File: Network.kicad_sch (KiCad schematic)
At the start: 32 parts, among them J6 RJ45_HR913550A, U1 IMX6UL, U11 RTL8201F

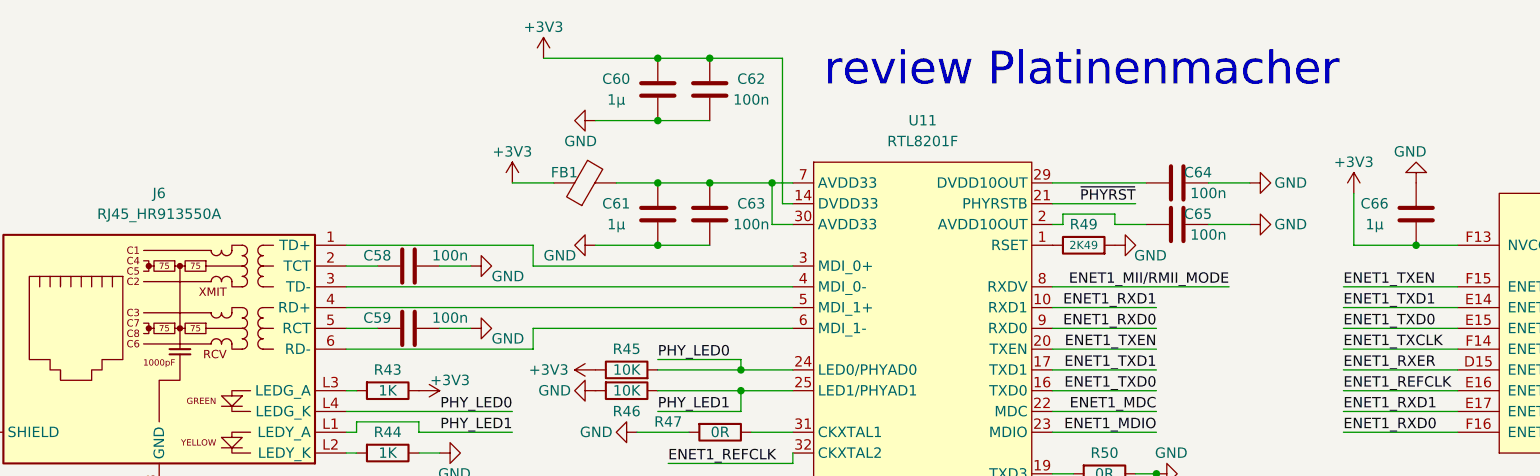
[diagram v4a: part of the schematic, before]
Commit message: update DDR
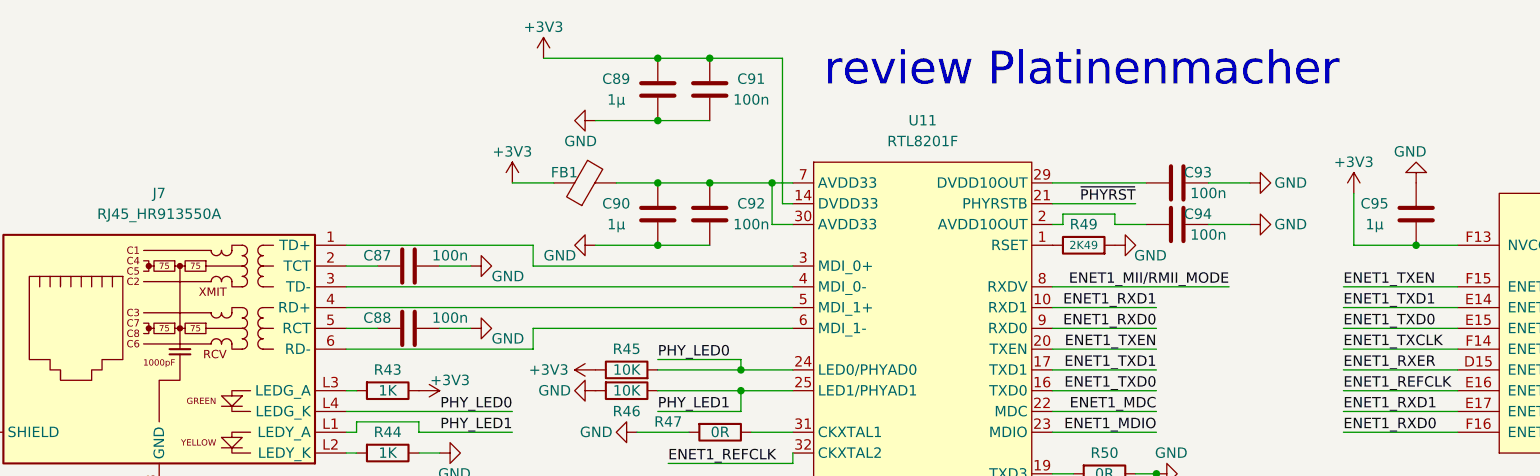
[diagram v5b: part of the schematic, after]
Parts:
- renumbered C58 to C87, C59 to C88, C60 to C89, C61 to C90, C62 to C91, C63 to C92, C64 to C93, C65 to C94, C66 to C95, J6 to J7
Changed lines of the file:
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@@
   (symbol (lib_id "power:GND") (at 193.04 54.61 180) (unit 1)
     (in_bom yes) (on_board yes)
-    (property "Reference" "#PWR0106" (id 0) (at 193.04 48.26 0)
+    (property "Reference" "#PWR0114" (id 0) (at 193.04 48.26 0)
       (effects (font (size 1.27 1.27)) hide)
     )
@@
   (symbol (lib_id "Connector:RJ45_Bel_SI-60062-F") (at 39.37 74.93 0) (mirror y) (unit 1)
     (in_bom yes) (on_board yes) (fields_autoplaced)
-    (property "Reference" "J6" (id 0) (at 39.37 55.88 0))
+    (property "Reference" "J7" (id 0) (at 39.37 55.88 0))
     (property "Value" "RJ45_HR913550A" (id 1) (at 39.37 58.42 0))
     (property "Footprint" "TheBrutzlers_Lib:RJ45_HR913550A" (id 2) (at 39.37 57.15 0)
@@
   (symbol (lib_id "power:GND") (at 73.66 87.63 90) (unit 1)
     (in_bom yes) (on_board yes)
-    (property "Reference" "#PWR090" (id 0) (at 80.01 87.63 0)
+    (property "Reference" "#PWR098" (id 0) (at 80.01 87.63 0)
       (effects (font (size 1.27 1.27)) hide)
     )
@@
   (symbol (lib_id "power:GND") (at 114.3 100.33 270) (unit 1)
     (in_bom yes) (on_board yes)
-    (property "Reference" "#PWR0100" (id 0) (at 107.95 100.33 0)
+    (property "Reference" "#PWR0108" (id 0) (at 107.95 100.33 0)
       (effects (font (size 1.27 1.27)) hide)
     )
@@
   (symbol (lib_id "power:GND") (at 172.72 59.69 90) (unit 1)
     (in_bom yes) (on_board yes)
-    (property "Reference" "#PWR0104" (id 0) (at 179.07 59.69 0)
+    (property "Reference" "#PWR0112" (id 0) (at 179.07 59.69 0)
       (effects (font (size 1.27 1.27)) hide)
     )
@@
   (symbol (lib_id "power:+3V3") (at 205.74 97.79 0) (unit 1)
     (in_bom yes) (on_board yes)
-    (property "Reference" "#PWR0107" (id 0) (at 205.74 101.6 0)
+    (property "Reference" "#PWR0115" (id 0) (at 205.74 101.6 0)
       (effects (font (size 1.27 1.27)) hide)
     )
@@
   (symbol (lib_id "power:GND") (at 172.72 54.61 90) (unit 1)
     (in_bom yes) (on_board yes)
-    (property "Reference" "#PWR0103" (id 0) (at 179.07 54.61 0)
+    (property "Reference" "#PWR0111" (id 0) (at 179.07 54.61 0)
       (effects (font (size 1.27 1.27)) hide)
     )
@@
   (symbol (lib_id "power:+3V3") (at 86.36 39.37 0) (unit 1)
     (in_bom yes) (on_board yes)
-    (property "Reference" "#PWR094" (id 0) (at 86.36 43.18 0)
+    (property "Reference" "#PWR0102" (id 0) (at 86.36 43.18 0)
       (effects (font (size 1.27 1.27)) hide)
     )
@@
   (symbol (lib_id "Device:C") (at 106.68 43.18 180) (unit 1)
     (in_bom yes) (on_board yes)
-    (property "Reference" "C62" (id 0) (at 111.76 41.91 0))
+    (property "Reference" "C91" (id 0) (at 111.76 41.91 0))
     (property "Value" "100n" (id 1) (at 111.76 44.45 0))
     (property "Footprint" "Capacitor_SMD:C_0402_1005Metric" (id 2) (at 105.7148 39.37 0)
@@
   (symbol (lib_id "Device:C") (at 163.83 59.69 270) (unit 1)
     (in_bom yes) (on_board yes)
-    (property "Reference" "C65" (id 0) (at 166.37 58.42 90))
+    (property "Reference" "C94" (id 0) (at 166.37 58.42 90))
     (property "Value" "100n" (id 1) (at 167.64 60.96 90))
     (property "Footprint" "Capacitor_SMD:C_0402_1005Metric" (id 2) (at 160.02 60.6552 0)
@@
   (symbol (lib_id "Device:C") (at 106.68 58.42 180) (unit 1)
     (in_bom yes) (on_board yes)
-    (property "Reference" "C63" (id 0) (at 111.76 57.15 0))
+    (property "Reference" "C92" (id 0) (at 111.76 57.15 0))
     (property "Value" "100n" (id 1) (at 111.76 59.69 0))
     (property "Footprint" "Capacitor_SMD:C_0402_1005Metric" (id 2) (at 105.7148 54.61 0)
@@
   (symbol (lib_id "Device:C") (at 100.33 43.18 180) (unit 1)
     (in_bom yes) (on_board yes)
-    (property "Reference" "C60" (id 0) (at 95.25 41.91 0))
+    (property "Reference" "C89" (id 0) (at 95.25 41.91 0))
     (property "Value" "1µ" (id 1) (at 95.25 44.45 0))
     (property "Footprint" "Capacitor_SMD:C_0402_1005Metric" (id 2) (at 99.3648 39.37 0)
@@
   (symbol (lib_id "Device:C") (at 100.33 58.42 180) (unit 1)
     (in_bom yes) (on_board yes)
-    (property "Reference" "C61" (id 0) (at 95.25 57.15 0))
+    (property "Reference" "C90" (id 0) (at 95.25 57.15 0))
     (property "Value" "1µ" (id 1) (at 95.25 59.69 0))
     (property "Footprint" "Capacitor_SMD:C_0402_1005Metric" (id 2) (at 99.3648 54.61 0)
@@
   (symbol (lib_id "power:+3V3") (at 92.71 77.47 90) (unit 1)
     (in_bom yes) (on_board yes)
-    (property "Reference" "#PWR097" (id 0) (at 96.52 77.47 0)
+    (property "Reference" "#PWR0105" (id 0) (at 96.52 77.47 0)
       (effects (font (size 1.27 1.27)) hide)
     )
@@
   (symbol (lib_id "power:+3V3") (at 185.42 55.88 0) (unit 1)
     (in_bom yes) (on_board yes)
-    (property "Reference" "#PWR0105" (id 0) (at 185.42 59.69 0)
+    (property "Reference" "#PWR0113" (id 0) (at 185.42 59.69 0)
       (effects (font (size 1.27 1.27)) hide)
     )
@@
   (symbol (lib_id "power:GND") (at 16.51 85.09 0) (unit 1)
     (in_bom yes) (on_board yes)
-    (property "Reference" "#PWR087" (id 0) (at 16.51 91.44 0)
+    (property "Reference" "#PWR095" (id 0) (at 16.51 91.44 0)
       (effects (font (size 1.27 1.27)) hide)
     )
@@
   (symbol (lib_id "power:GND") (at 156.21 62.23 90) (unit 1)
     (in_bom yes) (on_board yes)
-    (property "Reference" "#PWR0101" (id 0) (at 162.56 62.23 0)
+    (property "Reference" "#PWR0109" (id 0) (at 162.56 62.23 0)
       (effects (font (size 1.27 1.27)) hide)
     )
@@
   (symbol (lib_id "Device:C") (at 193.04 58.42 180) (unit 1)
     (in_bom yes) (on_board yes)
-    (property "Reference" "C66" (id 0) (at 187.96 57.15 0))
+    (property "Reference" "C95" (id 0) (at 187.96 57.15 0))
     (property "Value" "1µ" (id 1) (at 187.96 59.69 0))
     (property "Footprint" "Capacitor_SMD:C_0402_1005Metric" (id 2) (at 192.0748 54.61 0)
@@
   (symbol (lib_id "power:GND") (at 92.71 46.99 270) (unit 1)
     (in_bom yes) (on_board yes)
-    (property "Reference" "#PWR095" (id 0) (at 86.36 46.99 0)
+    (property "Reference" "#PWR0103" (id 0) (at 86.36 46.99 0)
       (effects (font (size 1.27 1.27)) hide)
     )
@@
   (symbol (lib_id "power:GND") (at 39.37 92.71 0) (unit 1)
     (in_bom yes) (on_board yes)
-    (property "Reference" "#PWR088" (id 0) (at 39.37 99.06 0)
+    (property "Reference" "#PWR096" (id 0) (at 39.37 99.06 0)
       (effects (font (size 1.27 1.27)) hide)
     )
@@
   (symbol (lib_id "power:GND") (at 205.74 127 0) (unit 1)
     (in_bom yes) (on_board yes)
-    (property "Reference" "#PWR0108" (id 0) (at 205.74 133.35 0)
+    (property "Reference" "#PWR0116" (id 0) (at 205.74 133.35 0)
       (effects (font (size 1.27 1.27)) hide)
     )
@@
   (symbol (lib_id "power:GND") (at 77.47 64.77 90) (unit 1)
     (in_bom yes) (on_board yes)
-    (property "Reference" "#PWR091" (id 0) (at 83.82 64.77 0)
+    (property "Reference" "#PWR099" (id 0) (at 83.82 64.77 0)
       (effects (font (size 1.27 1.27)) hide)
     )
@@
   (symbol (lib_id "power:+3V3") (at 71.12 80.01 270) (unit 1)
     (in_bom yes) (on_board yes)
-    (property "Reference" "#PWR089" (id 0) (at 67.31 80.01 0)
+    (property "Reference" "#PWR097" (id 0) (at 67.31 80.01 0)
       (effects (font (size 1.27 1.27)) hide)
     )
@@
   (symbol (lib_id "power:GND") (at 97.79 85.09 270) (unit 1)
     (in_bom yes) (on_board yes)
-    (property "Reference" "#PWR099" (id 0) (at 91.44 85.09 0)
+    (property "Reference" "#PWR0107" (id 0) (at 91.44 85.09 0)
       (effects (font (size 1.27 1.27)) hide)
     )
@@
   (symbol (lib_id "power:GND") (at 92.71 80.01 270) (unit 1)
     (in_bom yes) (on_board yes)
-    (property "Reference" "#PWR098" (id 0) (at 86.36 80.01 0)
+    (property "Reference" "#PWR0106" (id 0) (at 86.36 80.01 0)
       (effects (font (size 1.27 1.27)) hide)
     )
@@
   (symbol (lib_id "Device:C") (at 163.83 54.61 270) (unit 1)
     (in_bom yes) (on_board yes)
-    (property "Reference" "C64" (id 0) (at 166.37 53.34 90))
+    (property "Reference" "C93" (id 0) (at 166.37 53.34 90))
     (property "Value" "100n" (id 1) (at 167.64 55.88 90))
     (property "Footprint" "Capacitor_SMD:C_0402_1005Metric" (id 2) (at 160.02 55.5752 0)
@@
   (symbol (lib_id "power:+3V3") (at 82.55 54.61 0) (unit 1)
     (in_bom yes) (on_board yes)
-    (property "Reference" "#PWR093" (id 0) (at 82.55 58.42 0)
+    (property "Reference" "#PWR0101" (id 0) (at 82.55 58.42 0)
       (effects (font (size 1.27 1.27)) hide)
     )
@@
   (symbol (lib_id "Device:C") (at 69.85 72.39 90) (unit 1)
     (in_bom yes) (on_board yes)
-    (property "Reference" "C59" (id 0) (at 66.04 71.12 90))
+    (property "Reference" "C88" (id 0) (at 66.04 71.12 90))
     (property "Value" "100n" (id 1) (at 74.93 71.12 90))
     (property "Footprint" "Capacitor_SMD:C_0402_1005Metric" (id 2) (at 73.66 71.4248 0)
@@
   (symbol (lib_id "Device:C") (at 69.85 64.77 90) (unit 1)
     (in_bom yes) (on_board yes)
-    (property "Reference" "C58" (id 0) (at 66.04 63.5 90))
+    (property "Reference" "C87" (id 0) (at 66.04 63.5 90))
     (property "Value" "100n" (id 1) (at 74.93 63.5 90))
     (property "Footprint" "Capacitor_SMD:C_0402_1005Metric" (id 2) (at 73.66 63.8048 0)
@@
   (symbol (lib_id "power:GND") (at 92.71 62.23 270) (unit 1)
     (in_bom yes) (on_board yes)
-    (property "Reference" "#PWR096" (id 0) (at 86.36 62.23 0)
+    (property "Reference" "#PWR0104" (id 0) (at 86.36 62.23 0)
       (effects (font (size 1.27 1.27)) hide)
     )
@@
   (symbol (lib_id "power:GND") (at 77.47 72.39 90) (unit 1)
     (in_bom yes) (on_board yes)
-    (property "Reference" "#PWR092" (id 0) (at 83.82 72.39 0)
+    (property "Reference" "#PWR0100" (id 0) (at 83.82 72.39 0)
       (effects (font (size 1.27 1.27)) hide)
     )
@@
   (symbol (lib_id "power:GND") (at 161.29 90.17 90) (unit 1)
     (in_bom yes) (on_board yes)
-    (property "Reference" "#PWR0102" (id 0) (at 167.64 90.17 0)
-      (effects (font (size 1.27 1.27)) hide)
-    )
+    (property "Reference" "#PWR0110" (id 0) (at 167.64 90.17 0)
+      (effects (font (size 1.27 1.27)) hide)
+    )
